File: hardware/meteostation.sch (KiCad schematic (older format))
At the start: 12 parts

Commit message: Changed atmega power to 3.3v instead of 5v Added type-c connector
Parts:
- C? (x2): value 12pF -> TBD
- J?: value Conn_02x03 -> ISP
- Y?: value 16MHz -> 8MHz; footprint Crystal:Crystal_SMD_3225-4Pin_3.2x2.5mm_HandSoldering -> (none)
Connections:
- net labels added: +3.3V
- net labels removed: +5V
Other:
- note added: "Capacitors for VCC \nand GND pins on MCU"
- note removed: "Capacitors for +5V \nand GND pins on MCU"
- note removed: "ISP Connector"
- moved on the sheet: C?
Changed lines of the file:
@@
 L Device:C C?
 U 1 1 6032A8FA
-P 9300 6000
-F 0 "C?" H 9415 6046 50  0000 L CNN
-F 1 "100nF" H 9415 5955 50  0000 L CNN
-F 2 "" H 9338 5850 50  0001 C CNN
-F 3 "~" H 9300 6000 50  0001 C CNN
-	1    9300 6000
+P 4950 1850
+F 0 "C?" H 5065 1896 50  0000 L CNN
+F 1 "100nF" H 5065 1805 50  0000 L CNN
+F 2 "" H 4988 1700 50  0001 C CNN
+F 3 "~" H 4950 1850 50  0001 C CNN
+	1    4950 1850
 	1    0    0    -1
 $EndComp
@@
 L power:GND #PWR0103
 U 1 1 6032C2F4
-P 9050 6150
-F 0 "#PWR0103" H 9050 5900 50  0001 C CNN
-F 1 "GND" H 9055 5977 50  0000 C CNN
-F 2 "" H 9050 6150 50  0001 C CNN
-F 3 "" H 9050 6150 50  0001 C CNN
-	1    9050 6150
-	1    0    0    -1
-$EndComp
-$Comp
-L power:+5V #PWR0104
-U 1 1 6032DE53
-P 9050 5850
-F 0 "#PWR0104" H 9050 5700 50  0001 C CNN
-F 1 "+5V" H 9065 6023 50  0000 C CNN
-F 2 "" H 9050 5850 50  0001 C CNN
-F 3 "" H 9050 5850 50  0001 C CNN
-	1    9050 5850
+P 4700 2000
+F 0 "#PWR0103" H 4700 1750 50  0001 C CNN
+F 1 "GND" H 4705 1827 50  0000 C CNN
+F 2 "" H 4700 2000 50  0001 C CNN
+F 3 "" H 4700 2000 50  0001 C CNN
+	1    4700 2000
 	1    0    0    -1
 $EndComp
@@
 L Device:C C?
 U 1 1 60328012
-P 8800 6000
-F 0 "C?" H 8915 6046 50  0000 L CNN
-F 1 "100nF" H 8915 5955 50  0000 L CNN
-F 2 "" H 8838 5850 50  0001 C CNN
-F 3 "~" H 8800 6000 50  0001 C CNN
-	1    8800 6000
-	1    0    0    -1
-$EndComp
-Wire Wire Line
-	8800 5850 9050 5850
-Connection ~ 9050 5850
-Wire Wire Line
-	9050 5850 9300 5850
-Wire Wire Line
-	8800 6150 9050 6150
-Connection ~ 9050 6150
-Wire Wire Line
-	9050 6150 9300 6150
+P 4450 1850
+F 0 "C?" H 4565 1896 50  0000 L CNN
+F 1 "100nF" H 4565 1805 50  0000 L CNN
+F 2 "" H 4488 1700 50  0001 C CNN
+F 3 "~" H 4450 1850 50  0001 C CNN
+	1    4450 1850
+	1    0    0    -1
+$EndComp
+Wire Wire Line
+	4450 2000 4700 2000
+Connection ~ 4700 2000
+Wire Wire Line
+	4700 2000 4950 2000
 Wire Notes Line
-	8650 5600 9700 5600
+	4300 1450 5350 1450
 Wire Notes Line
-	9700 5600 9700 6400
+	5350 1450 5350 2250
 Wire Notes Line
-	9700 6400 8650 6400
+	5350 2250 4300 2250
 Wire Notes Line
-	8650 6400 8650 5600
-Text Notes 8750 5600 0    50   ~ 0
-Capacitors for +5V \nand GND pins on MCU
+	4300 2250 4300 1450
+Text Notes 4400 1450 0    50   ~ 0
+Capacitors for VCC \nand GND pins on MCU
 $Comp
 L Device:L L?
@@
 	1    0    0    -1
 $EndComp
-$Comp
-L power:+5V #PWR0105
-U 1 1 60350996
-P 5800 2050
-F 0 "#PWR0105" H 5800 1900 50  0001 C CNN
-F 1 "+5V" H 5815 2223 50  0000 C CNN
-F 2 "" H 5800 2050 50  0001 C CNN
-F 3 "" H 5800 2050 50  0001 C CNN
-	1    5800 2050
-	1    0    0    -1
-$EndComp
 Wire Wire Line
 	5850 2150 5850 2050
 Wire Wire Line
-	5850 2050 5800 2050
-Wire Wire Line
-	5800 2050 5750 2050
-Wire Wire Line
 	5750 2050 5750 2450
-Connection ~ 5800 2050
 $Comp
 L Device:R R?
@@
 $EndComp
 $Comp
-L power:+5V #PWR0106
-U 1 1 60355BB2
-P 8050 4250
-F 0 "#PWR0106" H 8050 4100 50  0001 C CNN
-F 1 "+5V" H 8065 4423 50  0000 C CNN
-F 2 "" H 8050 4250 50  0001 C CNN
-F 3 "" H 8050 4250 50  0001 C CNN
-	1    8050 4250
-	1    0    0    -1
-$EndComp
-$Comp
 L Switch:SW_MEC_5G SW?
 U 1 1 6035A760
@@
 P 7200 3350
 F 0 "Y?" V 7154 3594 50  0000 L CNN
-F 1 "16MHz" V 7245 3594 50  0000 L CNN
-F 2 "Crystal:Crystal_SMD_3225-4Pin_3.2x2.5mm_HandSoldering" H 7200 3350 50  0001 C CNN
-F 3 "https://lcsc.com/product-detail/SMD-Crystal-Resonators_Seiko-Epson-X1E000021061300_C255909.html" H 7200 3350 50  0001 C CNN
+F 1 "8MHz" V 7245 3594 50  0000 L CNN
+F 2 "" H 7200 3350 50  0001 C CNN
+F 3 "" H 7200 3350 50  0001 C CNN
 	1    7200 3350
 	0    1    1    0
@@
 P 7800 3500
 F 0 "C?" V 7650 3500 50  0000 C CNN
-F 1 "12pF" V 7750 3650 50  0000 C CNN
+F 1 "TBD" V 7750 3650 50  0000 C CNN
 F 2 "" H 7838 3350 50  0001 C CNN
 F 3 "~" H 7800 3500 50  0001 C CNN
@@
 P 7800 3200
 F 0 "C?" V 7650 3200 50  0000 C CNN
-F 1 "12pF" V 7750 3350 50  0000 C CNN
+F 1 "TBD" V 7750 3350 50  0000 C CNN
 F 2 "" H 7838 3050 50  0001 C CNN
 F 3 "~" H 7800 3200 50  0001 C CNN
@@
 L Connector_Generic:Conn_02x03_Odd_Even J?
 U 1 1 60390A7D
-P 10350 6050
-F 0 "J?" H 10400 6250 50  0000 C CNN
-F 1 "Conn_02x03" H 10350 5850 50  0000 C CNN
-F 2 "" H 10350 6050 50  0001 C CNN
-F 3 "~" H 10350 6050 50  0001 C CNN
-	1    10350 6050
-	1    0    0    -1
-$EndComp
-$Comp
-L power:+5V #PWR0109
-U 1 1 60391EBC
-P 10650 5950
-F 0 "#PWR0109" H 10650 5800 50  0001 C CNN
-F 1 "+5V" H 10665 6123 50  0000 C CNN
-F 2 "" H 10650 5950 50  0001 C CNN
-F 3 "" H 10650 5950 50  0001 C CNN
-	1    10650 5950
+P 5700 6200
+F 0 "J?" H 5750 6400 50  0000 C CNN
+F 1 "ISP" H 5700 6000 50  0000 C CNN
+F 2 "" H 5700 6200 50  0001 C CNN
+F 3 "~" H 5700 6200 50  0001 C CNN
+	1    5700 6200
 	1    0    0    -1
 $EndComp
@@
 L power:GND #PWR0110
 U 1 1 603933E2
-P 10650 6150
-F 0 "#PWR0110" H 10650 5900 50  0001 C CNN
-F 1 "GND" H 10655 5977 50  0000 C CNN
-F 2 "" H 10650 6150 50  0001 C CNN
-F 3 "" H 10650 6150 50  0001 C CNN
-	1    10650 6150
+P 6000 6300
+F 0 "#PWR0110" H 6000 6050 50  0001 C CNN
+F 1 "GND" H 6005 6127 50  0000 C CNN
+F 2 "" H 6000 6300 50  0001 C CNN
+F 3 "" H 6000 6300 50  0001 C CNN
+	1    6000 6300
 	1    0    0    -1
 $EndComp
@@
 Wire Wire Line
 	6350 3050 6500 3050
-Text Label 10800 6050 0    50   ~ 0
+Text Label 6150 6200 0    50   ~ 0
 MOSI
 Wire Wire Line
-	10800 6050 10650 6050
-Text Label 9950 5950 0    50   ~ 0
+	6150 6200 6000 6200
+Text Label 5300 6100 0    50   ~ 0
 MISO
 Wire Wire Line
-	10150 5950 9950 5950
-Text Label 9950 6050 0    50   ~ 0
+	5500 6100 5300 6100
+Text Label 5300 6200 0    50   ~ 0
 SCK
-Text Label 9950 6150 0    50   ~ 0
+Text Label 5300 6300 0    50   ~ 0
 RESET
 Wire Wire Line
-	9950 6150 10150 6150
-Wire Wire Line
-	9950 6050 10150 6050
+	5300 6300 5500 6300
+Wire Wire Line
+	5300 6200 5500 6200
 Text Label 7600 4000 0    50   ~ 0
 RESET
 Wire Wire Line
 	7600 4000 7600 4250
-Wire Notes Line
-	9900 5700 9900 6400
-Wire Notes Line
-	9900 6400 11000 6400
-Wire Notes Line
-	11000 6400 11000 5700
-Wire Notes Line
-	11000 5700 9900 5700
-Text Notes 10150 5650 0    50   ~ 0
-ISP Connector
 Text Label 6500 3150 0    50   ~ 0
 MISO
@@
 S 1750 2250 900  600
 U 603656E0
-F0 "Power" 50
-F1 "power.sch" 50
+F0 "Power And Usb" 50
+F1 "power_and_usb.sch" 50
 $EndSheet
+Wire Wire Line
+	5750 2050 5800 2050
+$Comp
+L power:+3.3V #PWR?
+U 1 1 603A3097
+P 5800 2050
+F 0 "#PWR?" H 5800 1900 50  0001 C CNN
+F 1 "+3.3V" H 5815 2223 50  0000 C CNN
+F 2 "" H 5800 2050 50  0001 C CNN
+F 3 "" H 5800 2050 50  0001 C CNN
+	1    5800 2050
+	1    0    0    -1
+$EndComp
+Connection ~ 5800 2050
+Wire Wire Line
+	5800 2050 5850 2050
+$Comp
+L power:+3.3V #PWR?
+U 1 1 603A43C9
+P 8050 4250
+F 0 "#PWR?" H 8050 4100 50  0001 C CNN
+F 1 "+3.3V" H 8065 4423 50  0000 C CNN
+F 2 "" H 8050 4250 50  0001 C CNN
+F 3 "" H 8050 4250 50  0001 C CNN
+	1    8050 4250
+	1    0    0    -1
+$EndComp
+$Comp
+L power:+3.3V #PWR?
+U 1 1 603A4B64
+P 6000 6100
+F 0 "#PWR?" H 6000 5950 50  0001 C CNN
+F 1 "+3.3V" H 6015 6273 50  0000 C CNN
+F 2 "" H 6000 6100 50  0001 C CNN
+F 3 "" H 6000 6100 50  0001 C CNN
+	1    6000 6100
+	1    0    0    -1
+$EndComp
+Wire Wire Line
+	4450 1700 4700 1700
+$Comp
+L power:+3.3V #PWR?
+U 1 1 603A52DC
+P 4700 1700
+F 0 "#PWR?" H 4700 1550 50  0001 C CNN
+F 1 "+3.3V" H 4715 1873 50  0000 C CNN
+F 2 "" H 4700 1700 50  0001 C CNN
+F 3 "" H 4700 1700 50  0001 C CNN
+	1    4700 1700
+	1    0    0    -1
+$EndComp
+Connection ~ 4700 1700
+Wire Wire Line
+	4700 1700 4950 1700
 $EndSCHEMATC

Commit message: Finished routing USB type-c and battery charging IC
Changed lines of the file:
@@
 F3 "TX" O L 8300 1900 50
 F4 "RX" I L 8300 2000 50
-F5 "SPI_MISO" O R 9400 2000 50
-F6 "SPI_CLK" I R 9400 2100 50
-F7 "SPI_CS" I R 9400 2200 50
-F8 "SPI_MOSI" I R 9400 1900 50
+F5 "MISO" O R 9400 2000 50
+F6 "CLK" I R 9400 2100 50
+F7 "CS" I R 9400 2200 50
+F8 "MOSI" I R 9400 1900 50
 $EndSheet
 $Sheet
-S 1750 2250 900  600
+S 1750 2250 1150 700
 U 603656E0
-F0 "Power And Usb" 50
+F0 "Power and USB" 50
 F1 "power_and_usb.sch" 50
+F2 "Q_DISABLE" I R 2900 2450 50
+F3 "BQ25890_INT" I R 2900 2850 50
+F4 "Q_BOOST" I R 2900 2350 50
+F5 "BQ25890_SCL" B R 2900 2750 50
+F6 "BQ25890_SDA" B R 2900 2650 50
+F7 "CH340_TX" O L 1750 2550 50
+F8 "CH340_RX" I L 1750 2650 50
 $EndSheet
 Wire Wire Line

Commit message: Add cubemx project Changed MCU and PD scheme
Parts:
- removed C?: 100nF, symbol Device:C
- removed J?: ISP, symbol Connector_Generic:Conn_02x03_Odd_Even
- removed L?: 10uH, symbol Device:L
- removed U?: ATmega328PB-AU, Package_QFP:TQFP-32_7x7mm_P0.8mm, symbol MCU_Microchip_ATmega:ATmega328PB-AU
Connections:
- net labels removed: MISO, MOSI, SCK
- wire segments 41 -> 30
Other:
- moved on the sheet: C?, R?, SW?, Y?

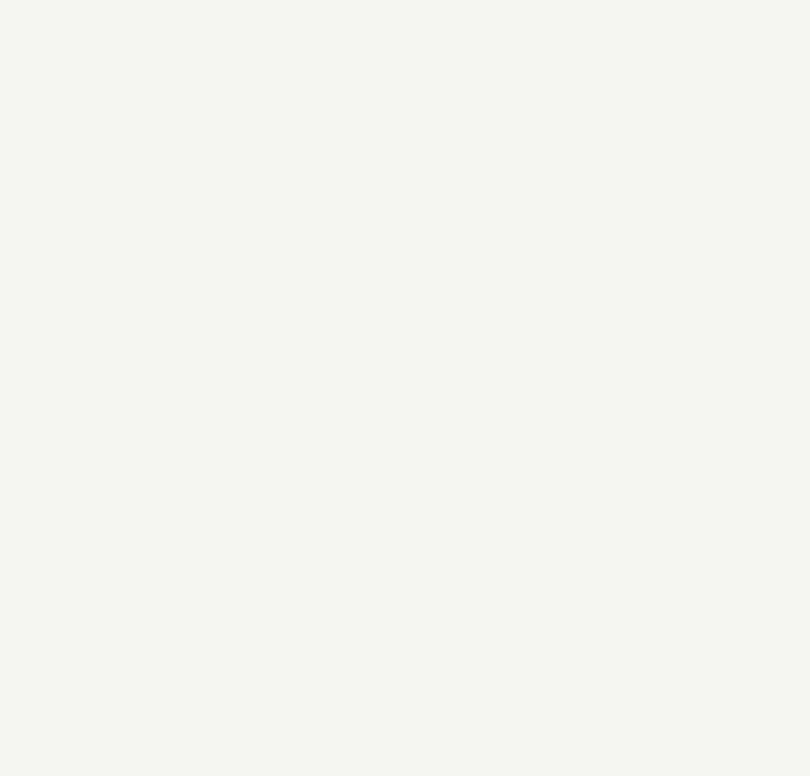
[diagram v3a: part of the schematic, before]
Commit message: Changed flash for esp8266 Added stm32 schematic
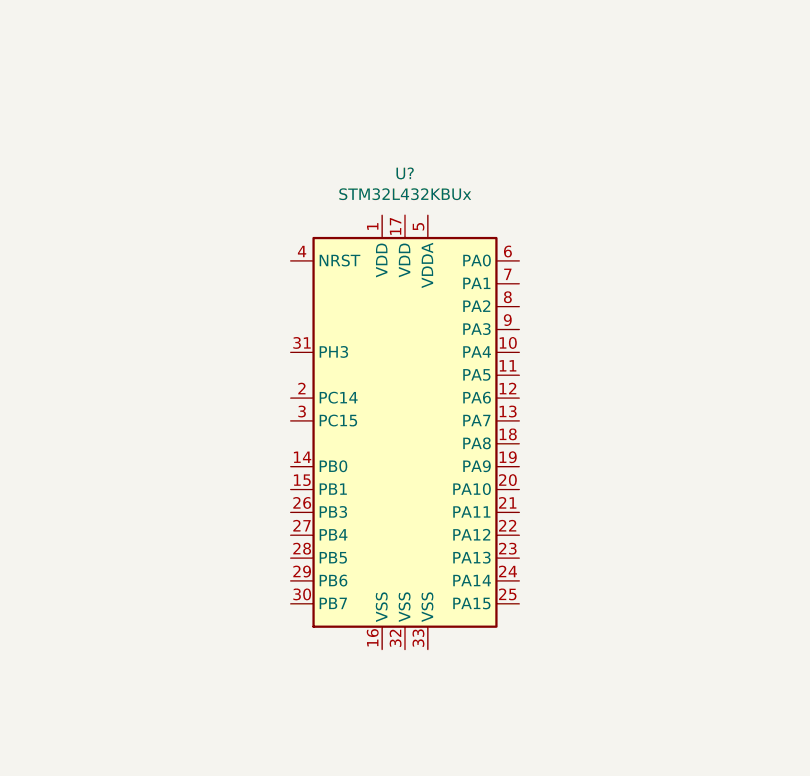
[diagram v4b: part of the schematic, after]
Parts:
- added U?: STM32L432KBUx, Package_DFN_QFN:QFN-32-1EP_5x5mm_P0.5mm_EP3.45x3.45mm, symbol MCU_ST_STM32L4:STM32L432KBUx
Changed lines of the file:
@@
 Wire Wire Line
 	2250 1050 2500 1050
+$Comp
+L MCU_ST_STM32L4:STM32L432KBUx U?
+U 1 1 604F928D
+P 5800 4150
+F 0 "U?" H 5800 5231 50  0000 C CNN
+F 1 "STM32L432KBUx" H 5800 5140 50  0000 C CNN
+F 2 "Package_DFN_QFN:QFN-32-1EP_5x5mm_P0.5mm_EP3.45x3.45mm" H 5400 3250 50  0001 R CNN
+F 3 "http://www.st.com/st-web-ui/static/active/en/resource/technical/document/datasheet/DM00257205.pdf" H 5800 4150 50  0001 C CNN
+	1    5800 4150
+	1    0    0    -1
+$EndComp
 $EndSCHEMATC

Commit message: Changing power circuit again
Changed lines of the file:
@@
 F8 "MOSI" I R 10500 1200 50
-$EndSheet
-$Sheet
-S 1750 2250 1150 700
-U 603656E0
-F0 "Power and USB" 50
-F1 "power_and_usb.sch" 50
-F2 "Q_DISABLE" I R 2900 2450 50
-F3 "BQ25890_INT" I R 2900 2850 50
-F4 "Q_BOOST" I R 2900 2350 50
-F5 "BQ25890_SCL" B R 2900 2750 50
-F6 "BQ25890_SDA" B R 2900 2650 50
-F7 "CH340_TX" O L 1750 2550 50
-F8 "CH340_RX" I L 1750 2650 50
 $EndSheet
 $Comp
@@
 	1    0    0    -1
 $EndComp
+$Sheet
+S 1750 2250 1150 700
+U 603656E0
+F0 "Power and USB" 50
+F1 "power_and_usb.sch" 50
+$EndSheet
 $EndSCHEMATC

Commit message: Finished power schematics
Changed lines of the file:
@@
 $Descr A4 11693 8268
 encoding utf-8
-Sheet 1 3
+Sheet 1 4
 Title "Meteostation"
 Date "2021-02-17"
@@
 $EndSheet
 $Comp
-L power:+3.3V #PWR?
+L power:+3.3V #PWR0101
 U 1 1 603A43C9
 P 9350 4700
-F 0 "#PWR?" H 9350 4550 50  0001 C CNN
+F 0 "#PWR0101" H 9350 4550 50  0001 C CNN
 F 1 "+3.3V" H 9365 4873 50  0000 C CNN
 F 2 "" H 9350 4700 50  0001 C CNN
@@
 	2000 1050 2250 1050
 $Comp
-L power:+3.3V #PWR?
+L power:+3.3V #PWR0102
 U 1 1 603A52DC
 P 2250 1050
-F 0 "#PWR?" H 2250 900 50  0001 C CNN
+F 0 "#PWR0102" H 2250 900 50  0001 C CNN
 F 1 "+3.3V" H 2265 1223 50  0000 C CNN
 F 2 "" H 2250 1050 50  0001 C CNN
@@
 $EndComp
 $Sheet
-S 1750 2250 1150 700
+S 1750 2250 1450 850
 U 603656E0
 F0 "Power and USB" 50
 F1 "power_and_usb.sch" 50
+F2 "BQ25895_INT" I L 1750 2600 50
+F3 "BQ25895_SCL" B L 1750 2500 50
+F4 "BQ25895_SDA" B L 1750 2400 50
+F5 "ChargeEnable" I L 1750 2700 50
+F6 "USB_D+" B R 3200 2850 50
+F7 "USB_D-" B R 3200 2950 50
+F8 "FUSB302_INT" I R 3200 2600 50
+F9 "FUSB302_SCL" B R 3200 2500 50
+F10 "FUSB302_SDA" B R 3200 2400 50
+$EndSheet
+$Sheet
+S 6800 1650 1300 950
+U 607D8CCB
+F0 "SX1278" 50
+F1 "sx1278.sch" 50
+$EndSheet
+$Sheet
+S 2050 4800 1050 850
+U 607D914A
+F0 "Sensors" 50
+F1 "sensors.sch" 50
 $EndSheet
 $EndSCHEMATC

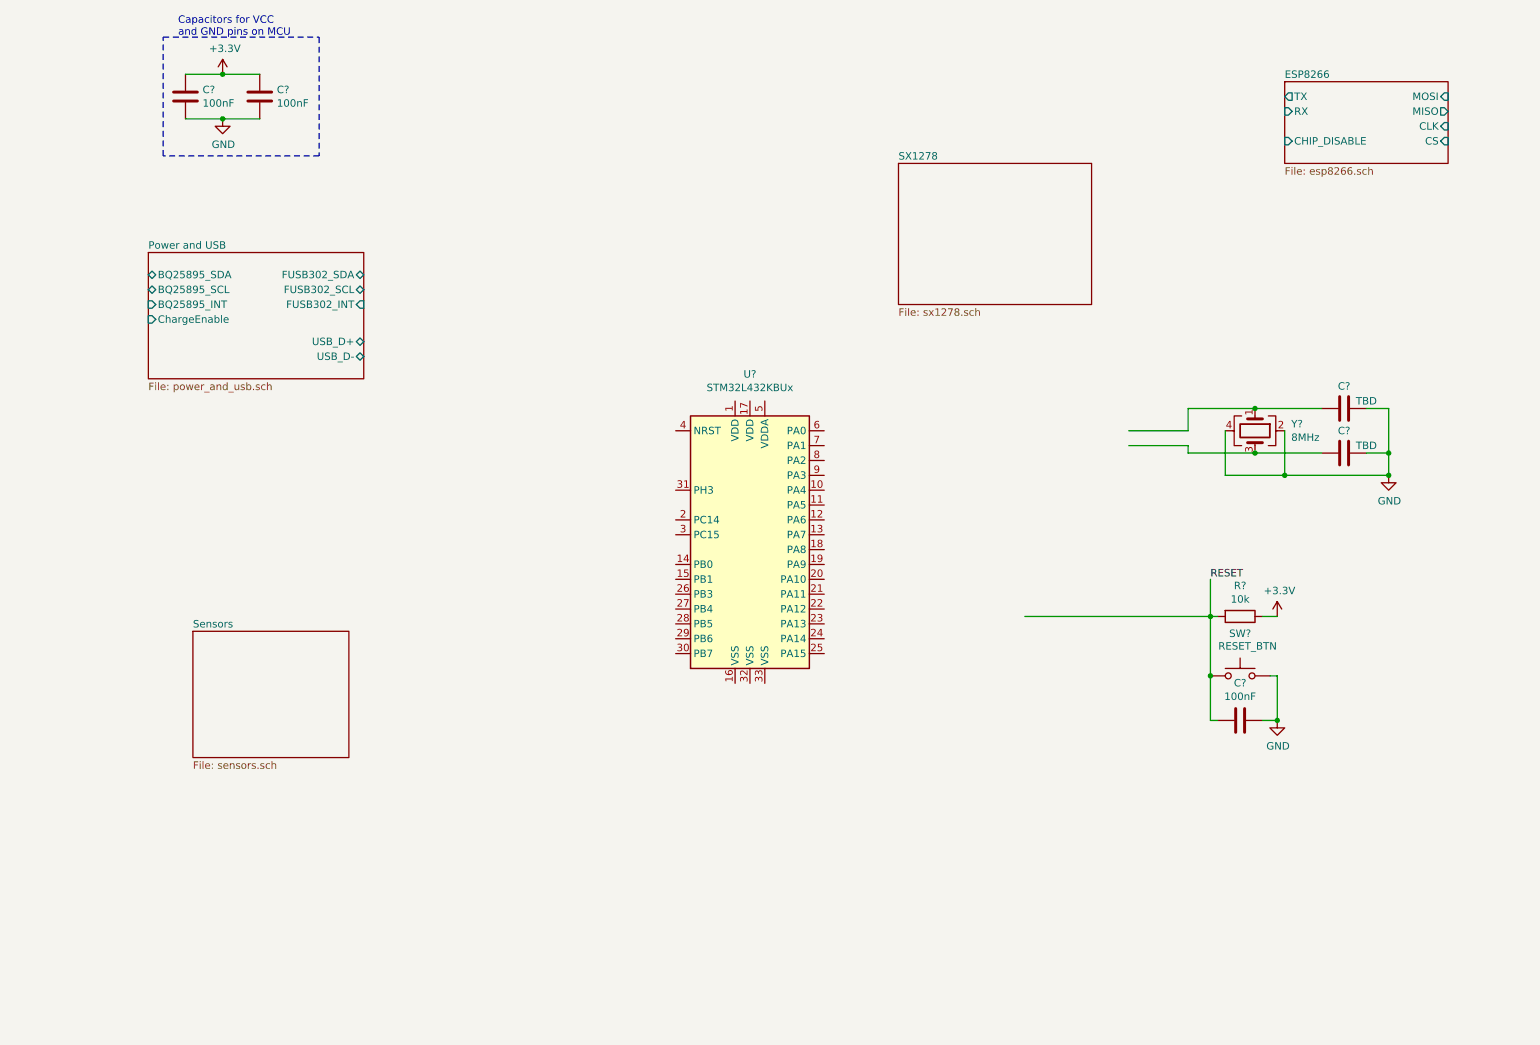
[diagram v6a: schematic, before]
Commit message: All sensors + most of MCU done
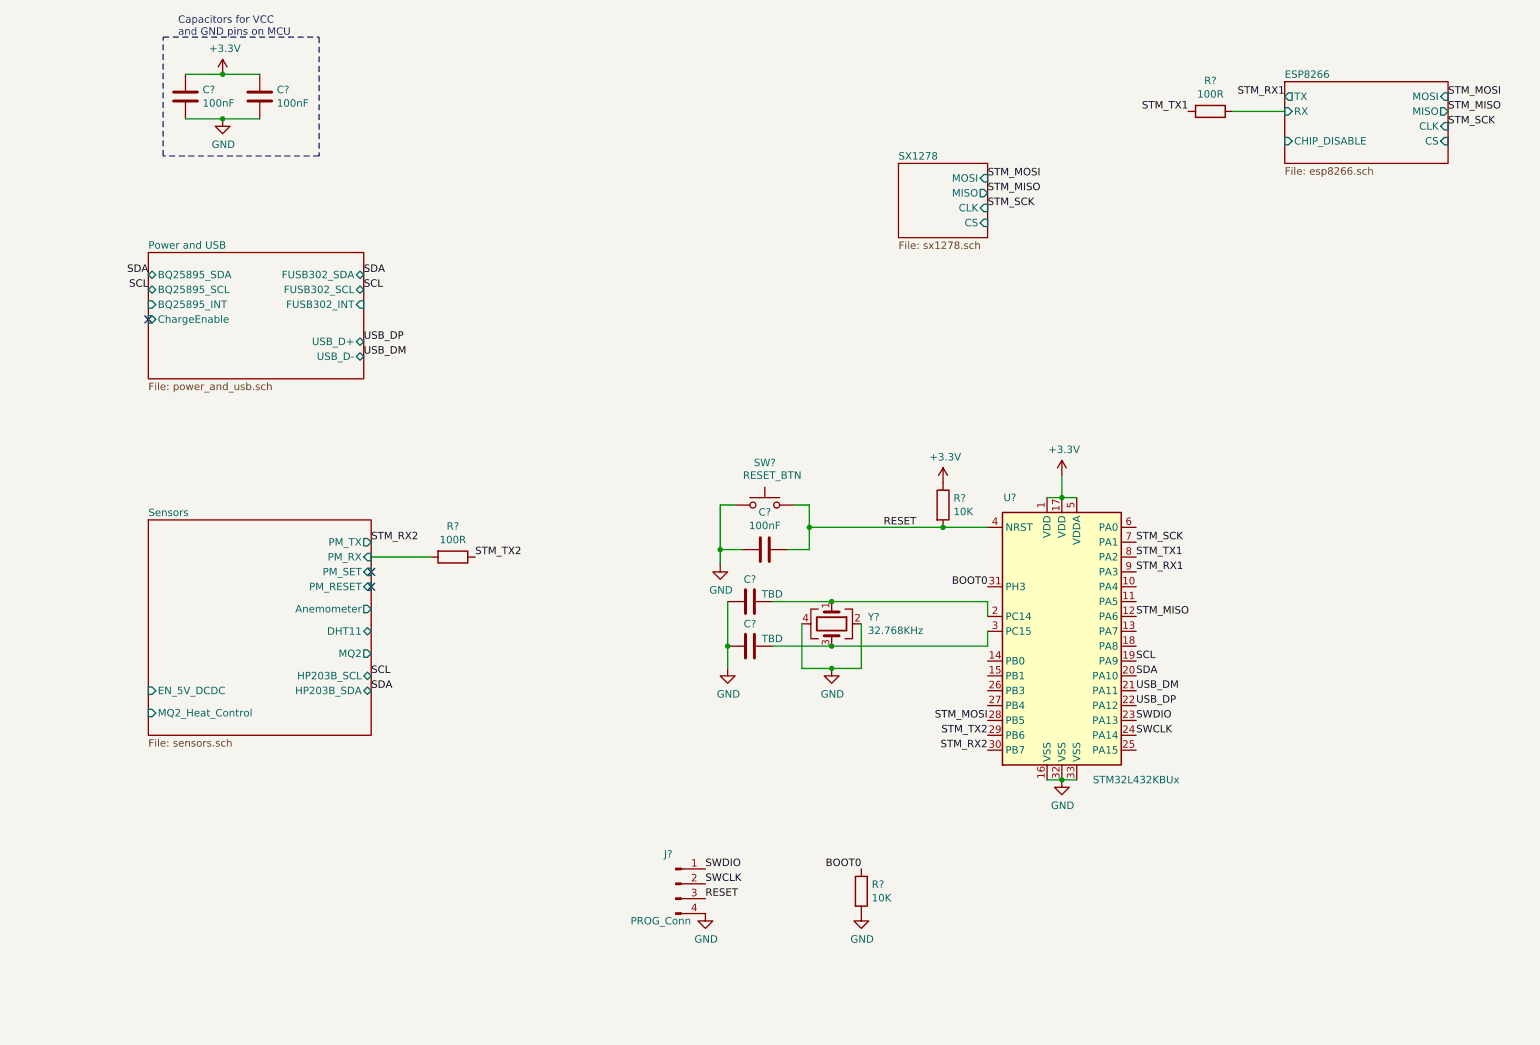
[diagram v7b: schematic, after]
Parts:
- removed C? (x2): TBD, symbol Device:C
- removed R?: 10k, symbol Device:R
- removed Y?: 8MHz, symbol Device:Crystal_GND24
- added C? (x2): TBD, symbol Device:C
- added J?: PROG_Conn, symbol Connector:Conn_01x04_Male
- added R? (x2): 100R, symbol Device:R
- added R? (x2): 10K, symbol Device:R
- added Y?: 32.768KHz, symbol Device:Crystal_GND24
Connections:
- net labels added: BOOT0, SCL, SDA, STM_MISO, STM_MOSI, STM_RX1, STM_RX2, STM_SCK, STM_TX1, STM_TX2, SWCLK, SWDIO, USB_DM, USB_DP
- wire segments 30 -> 33
- no-connect marks 0 -> 3
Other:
- moved on the sheet: C?, SW?, U?

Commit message: Finished main list
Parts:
- added C?: 100nF, symbol Device:C
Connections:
- net +3V3: now also C?.1
- net GND: now also C?.2
- net Anemometer: now reaches U?.10 (PA4)
- net DHT11: now reaches U?.11 (PA5)
- net MQ2: now reaches U?.13 (PA7)
- net LoRa_CS: now reaches U?.14 (PB0)
- net ESP_CS: now reaches U?.15 (PB1)
- net Enable_5V: now reaches U?.18 (PA8)
- net Enable_MQ2: now reaches U?.25 (PA15)
- net FUSB302_INT: now reaches U?.26 (PB3)
- net BQ25895_INT: now reaches U?.27 (PB4)
- net ESP_Disable: now reaches U?.6 (PA0)
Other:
- note removed: "Capacitors for VCC \nand GND pins on MCU"
- moved on the sheet: C?, J?, R?, SW?, U?, Y?
